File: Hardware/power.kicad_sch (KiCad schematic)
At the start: 14 parts, among them J3 XT30, U6 MP2331

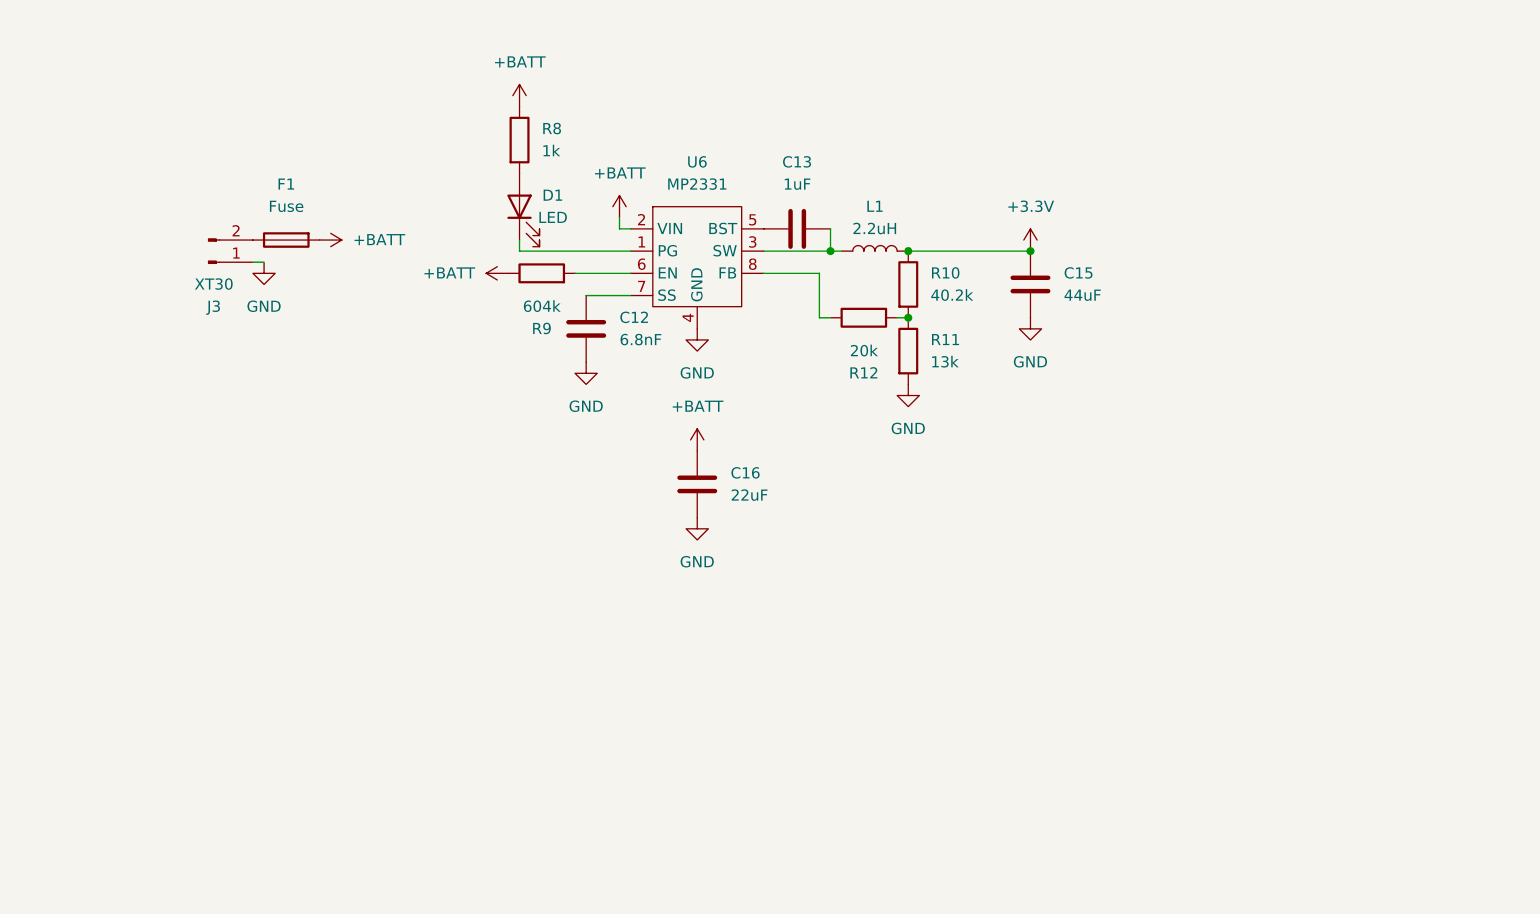
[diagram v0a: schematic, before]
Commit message: Changes in power system
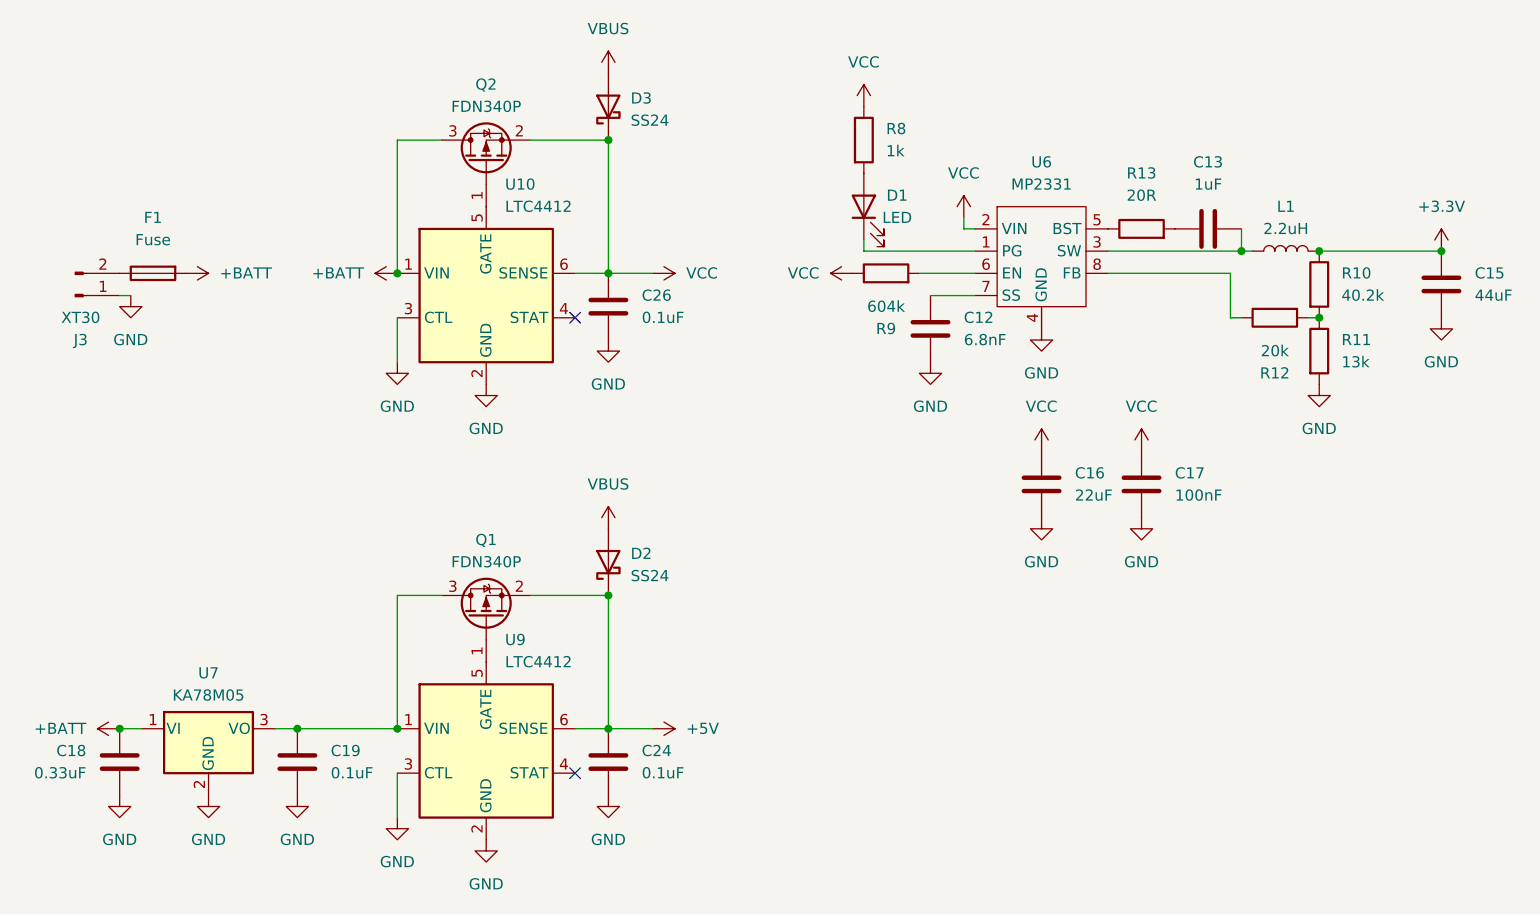
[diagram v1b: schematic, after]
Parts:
- added C17: 100nF, symbol Device:C
- added C18: 0.33uF, symbol Device:C
- added C19, C24, C26: 0.1uF, symbol Device:C
- added D2, D3: SS24, Diode_SMD:D_SMA, symbol Diode:SS24
- added Q1, Q2: FDN340P, Package_TO_SOT_SMD:SOT-23, symbol Transistor_FET:FDN340P
- added R13: 20R, symbol Device:R
- added U10, U9: LTC4412, Package_TO_SOT_SMD:TSOT-23-6, symbol Power_Management:LTC4412xS6
- added U7: KA78M05, Package_TO_SOT_SMD:TO-252-2, symbol Regulator_Linear:KA78M05_TO252
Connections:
- net +BATT: now also C18.1, Q2.3 (D), U10.1 (VIN), U7.1 (VI); no longer C16.1, R8.1, R9.1, U6.2 (VIN)
- net GND: now also C17.2, C18.2, C19.2, C24.2, C26.2, U10.2 (GND), U10.3 (CTL), U7.2 (GND), U9.2 (GND), U9.3 (CTL)
- net at U6.5 (BST): now also R13.1; no longer C13.1
- new net: Q1.1 (G), U9.5 (GATE)
- new net: C19.1, Q1.3 (D), U7.3 (VO), U9.1 (VIN)
- new net: C13.1, R13.2
- new net: Q2.1 (G), U10.5 (GATE)
- new net +5V: C24.1, D2.1 (K), Q1.2 (S), U9.6 (SENSE)
- new net VBUS: D2.2 (A), D3.2 (A)
- new net VCC: C16.1, C17.1, C26.1, D3.1 (K), Q2.2 (S), R8.1, R9.1, U10.6 (SENSE), U6.2 (VIN)
- no-connect marks 0 -> 2
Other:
- moved on the sheet: C12, C13, C15, C16, D1, F1, J3, L1, R10, R11, R12, R8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
